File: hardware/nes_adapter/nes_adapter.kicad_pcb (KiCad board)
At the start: 2 copper layers, 96.6 x 25.5 mm, 3 parts, among them J1 CART SLOT TOP ROW, J2 CART SLOT BOTTOM ROW, U1 NES_Slot

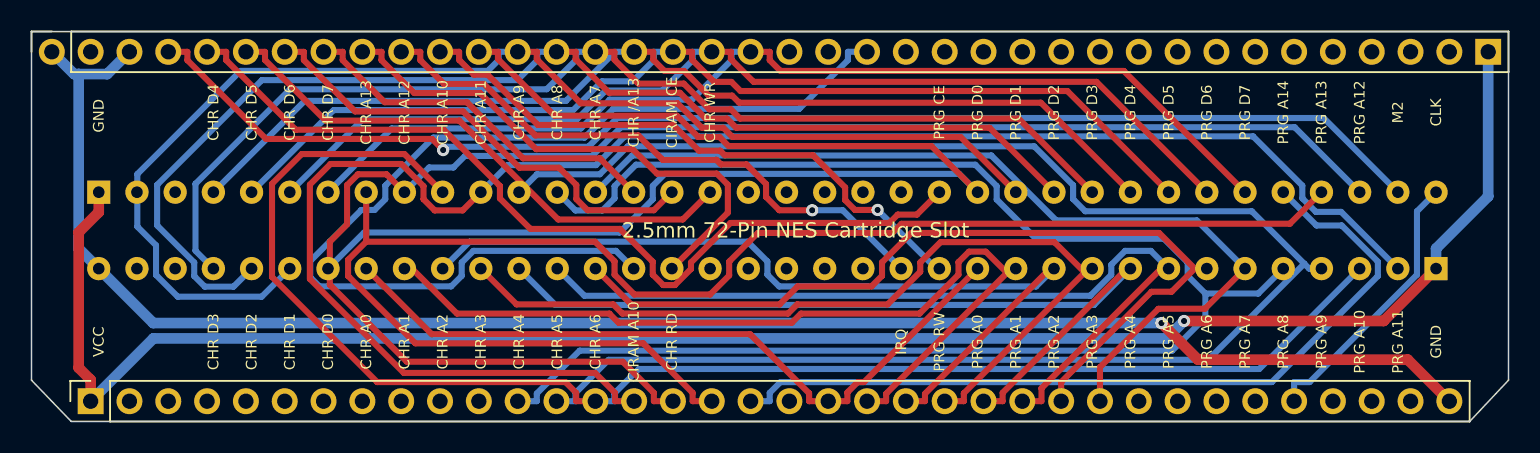
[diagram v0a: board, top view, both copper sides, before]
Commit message: Fix MD and NES adapter PCBs and add Famicom adapter
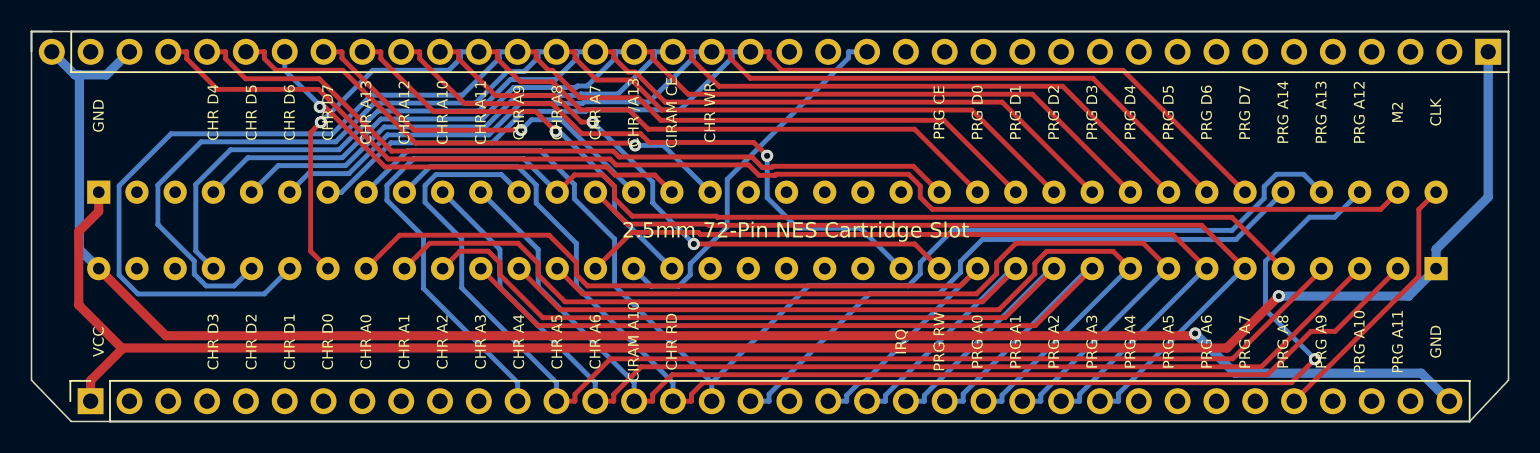
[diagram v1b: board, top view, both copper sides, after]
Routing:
- net D35: track 67.4 -> 24.6 mm
- net D25: track 110.6 -> 71.7 mm
- net D23: track 110.6 -> 78.6 mm
- net D24: track 97.8 -> 71.7 mm
- net A8: track 82.8 -> 59.5 mm, vias 0 -> 1
- net D22: track 104.0 -> 81.4 mm
- net D27: track 101.2 -> 80.5 mm
- net D26: track 103.5 -> 86.9 mm, vias 0 -> 1
- net D28: track 53.8 -> 41.2 mm
- net D49: track 47.8 -> 56.8 mm
- net A5: track 34.8 -> 27.3 mm, vias 0 -> 1
- net A1: track 58.3 -> 52.0 mm
- net D42: track 60.9 -> 57.9 mm
- net A9: track 82.4 -> 84.8 mm
- net D43: track 57.5 -> 55.4 mm
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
